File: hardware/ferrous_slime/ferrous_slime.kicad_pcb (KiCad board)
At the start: 2 copper layers, 41.4 x 34 mm, 50 parts, among them J1 IMU_Connector, J2 Battery_Connector, J3 USB_C_Receptacle_USB2.0, Q1 DMG3415U, SW1 SW_PWR, U1 BNO/MPU/ICM_Break, U2 ESP32-C3-MINI-1, U3 TP4056, U4 M3406, Y1 32.768Hz

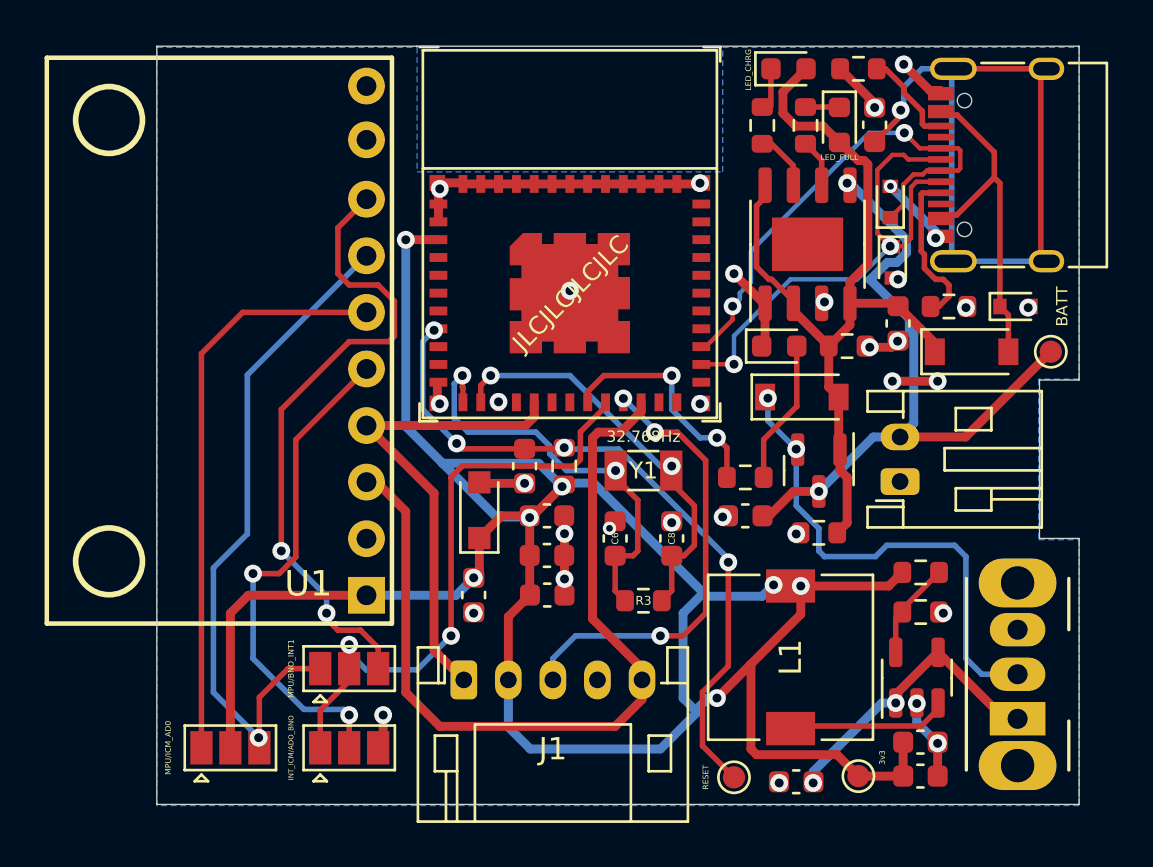
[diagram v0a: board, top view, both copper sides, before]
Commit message: Removed gerbers, made some minor tweaks to board layout
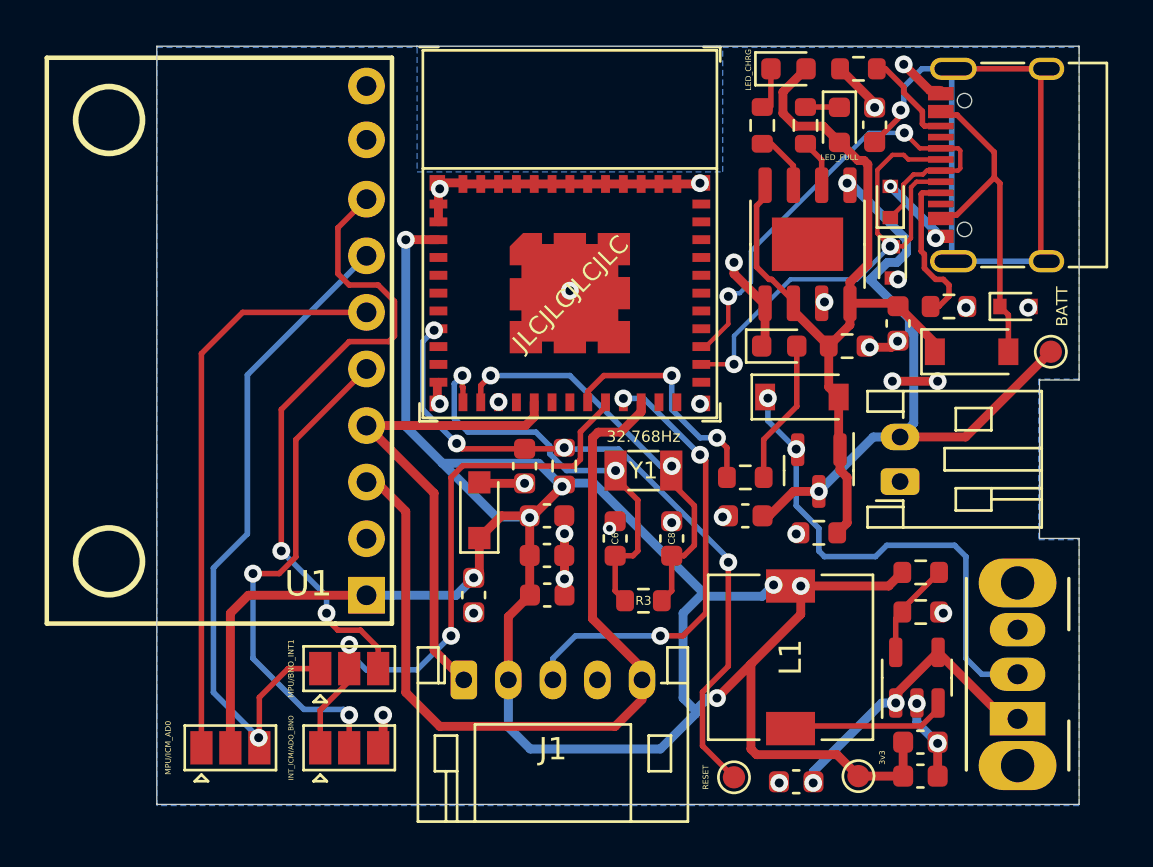
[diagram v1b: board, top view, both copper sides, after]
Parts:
- D5: value PROG_LED -> LED

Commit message: Optimized signal traces and ground fills
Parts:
- moved C4 6.07 mm to (67.5, 48.7), turned to -90 degrees
- moved J2 0.19 mm to (89.0, 49.3)
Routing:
- net USB_D+: track 22.4 -> 25.3 mm
- net USB_D-: track 22.6 -> 25.0 mm
- net GND: track 63.7 -> 65.0 mm, vias 32 -> 46
- net IO6_INT1: track 25.5 -> 26.6 mm
- net Net-(JP1-Pad3): track 30.9 -> 30.0 mm
- net IO8_SCL: track 37.0 -> 36.4 mm
- net +BATT: track 30.6 -> 30.7 mm, vias 2 -> 3
- net +3V3: track 109.8 -> 109.7 mm, vias 7 -> 8
- added copper zone on F.Cu, net GND
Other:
- outline, holes or cut-outs redrawn

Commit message: breakout_slime v0.1.2
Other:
- board text added: "${REVISION}"
- board text added: "ferrous_slime ${REVISION} by TheButlah License: CERN-OHL-P v2 or later github.com/TheButlah/slimevr_pcb"
- board text removed: "License: CERN-OHL-P v2 or later github.com/TheButlah/slimevr_pcb"
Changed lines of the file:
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@@
     (title "ferrous_slime")
     (date "2022-03-07")
+    (rev "v0.0.0")
     (company "github.com/thebutlah/slimevr_pcb")
     (comment 1 "Licensed under CERN-OHL-P v2 or later")
@@
       (xy 97.2312 29.919)
     ) (layer "Edge.Cuts") (width 0.05) (fill none))
-  (gr_text "License: CERN-OHL-P v2 or later\ngithub.com/TheButlah/slimevr_pcb" (at 58.166 44.196 90) (layer "B.SilkS")
+  (gr_text "ferrous_slime ${REVISION} by TheButlah\nLicense: CERN-OHL-P v2 or later\ngithub.com/TheButlah/slimevr_pcb\n" (at 58.801 44.069 90) (layer "B.SilkS")
     (effects (font (size 1 1) (thickness 0.2)) (justify mirror))
+  )
+  (gr_text "${REVISION}" (at 56.769 30.861 270) (layer "F.SilkS")
+    (effects (font (size 1 1) (thickness 0.2)) (justify left))
   )
   (gr_text "JLCJLCJLCJLC" (at 74.201188 41.015404 45) (layer "F.SilkS")
@@
     (pts (xy 97.028 29.919) (xy 55.626 29.919))
     (height 4.519)
-    (gr_text "41.4020 mm" (at 76.327 24.25) (layer "Dwgs.User")
+    (gr_text "1630.0000 mils" (at 76.327 24.25) (layer "Dwgs.User")
       (effects (font (size 1 1) (thickness 0.15)))
     )
@@
     (pts (xy 55.626 63.955) (xy 55.626 29.919))
     (height -9.906)
-    (gr_text "34.0360 mm" (at 44.57 46.937 90) (layer "Dwgs.User")
+    (gr_text "1340.0000 mils" (at 44.57 46.937 90) (layer "Dwgs.User")
       (effects (font (size 1 1) (thickness 0.15)))
     )
@@
     (pts (xy 97.028 29.919) (xy 50.52 29.972))
     (height 1.775074)
-    (gr_text "46.5080 mm" (at 73.770666 27.020428 0.06529360539) (layer "Dwgs.User")
-      (effects (font (size 1 1) (thickness 0.15)))
-    )
+    (gr_text "1831.0248 mils" (at 73.770666 27.020428 0.06529360539) (layer "Dwgs.User")
+      (effects (font (size 1 1) (thickness 0.15)))
+    )

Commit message: Added battery sense to ferrous_slime
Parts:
- removed C10: 470nF, Capacitor_SMD:C_0603_1608Metric
- added R12: 1M, Resistor_SMD:R_0603_1608Metric, F.Cu at (87.9, 33.5)
- added R13: 120K 1%, Resistor_SMD:R_0603_1608Metric, F.Cu at (72.5, 55.0)
- added R14: 30K 1%, Resistor_SMD:R_0603_1608Metric, F.Cu at (71.0, 55.0)
- R7: value 470R 1% -> 1K
- moved C5 10.2 mm to (60.0, 56.9), turned to 0 degrees
- moved C3 1.16 mm to (73.8, 51.8), turned to -90 degrees
- moved C1 1.10 mm to (74.2, 55.0), turned to 90 degrees
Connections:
- U2 pad 6: unconnected-(U2-Pad6) -> B_SENSE
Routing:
- net +BATT: track 30.7 -> 63.4 mm, vias 3 -> 5
- net B_SENSE: track 0.00 -> 17.6 mm, vias 0 -> 2
- net +3V3: track 109.7 -> 107.0 mm
- net GND: track 65.0 -> 65.8 mm
- net IO7_INT2: track 20.4 -> 21.0 mm

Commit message: Added breakouts for remaining unused IO
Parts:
- added J4: Unused_IO, Connector_PinHeader_2.54mm:PinHeader_1x07_P2.54mm_Vertical, F.Cu at (57.8, 34.4)
- R12: value 1M -> 120K
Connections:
- U2 pad 18: unconnected-(U2-Pad18) -> UNUSED_IO4
- U2 pad 23: unconnected-(U2-Pad23) -> UNUSED_IO9
- U2 pad 30: unconnected-(U2-Pad30) -> UNUSED_IO20
- U2 pad 31: unconnected-(U2-Pad31) -> UNUSED_IO21
- U2 pad 5: unconnected-(U2-Pad5) -> UNUSED_IO2
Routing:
- net UNUSED_IO21: track 0.00 -> 48.1 mm, vias 0 -> 2
- net UNUSED_IO20: track 0.00 -> 42.9 mm, vias 0 -> 1
- net UNUSED_IO9: track 0.00 -> 30.9 mm, vias 0 -> 2
- net UNUSED_IO4: track 0.00 -> 23.4 mm, vias 0 -> 1
- net UNUSED_IO2: track 0.00 -> 18.2 mm, vias 0 -> 2
- net +3V3: track 107.0 -> 122.9 mm
- net GND: track 65.8 -> 58.4 mm, vias 46 -> 48
- net Net-(C2-Pad1): track 30.9 -> 33.1 mm
- net IO0: track 18.6 -> 19.9 mm
- net Net-(JP1-Pad3): track 30.0 -> 31.3 mm
- net IO5_LED: track 10.6 -> 9.82 mm
- net IO7_INT2: track 21.0 -> 21.7 mm
- net Net-(JP1-Pad1): track 25.9 -> 25.3 mm

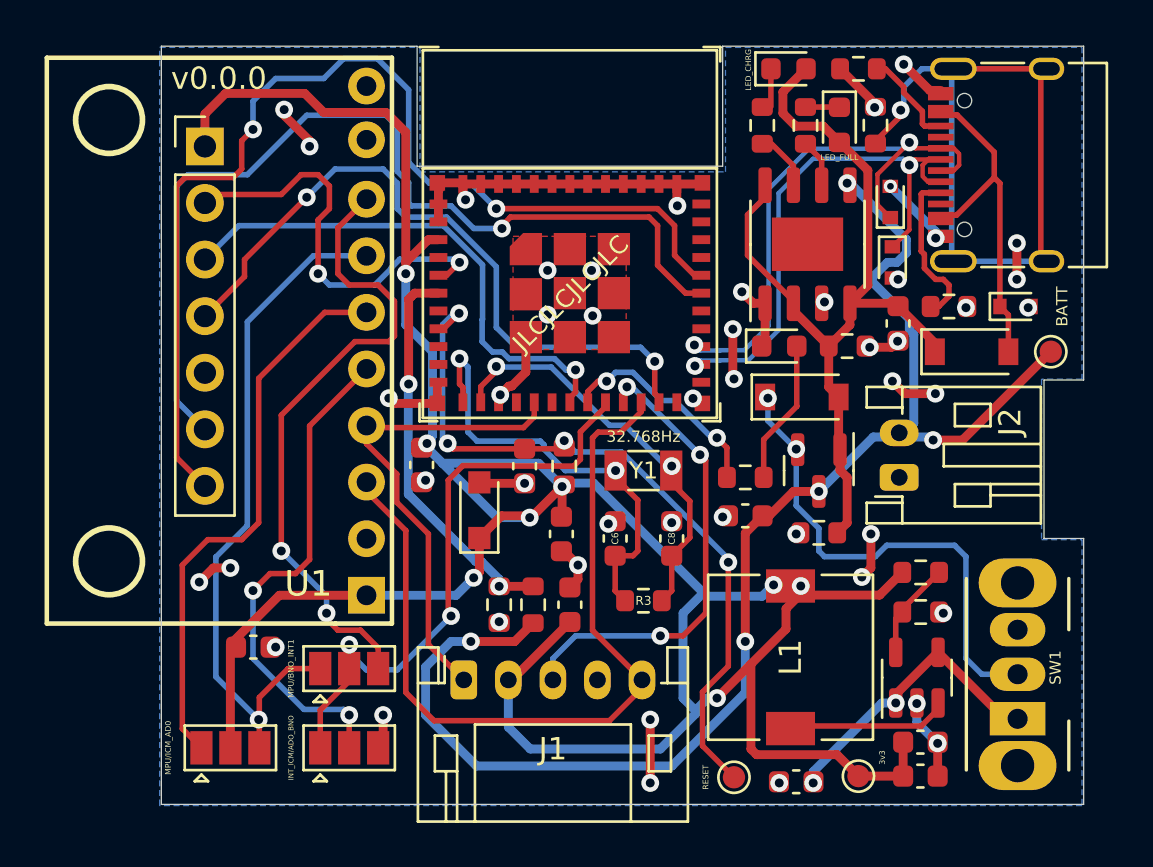
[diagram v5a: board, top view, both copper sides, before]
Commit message: Fixed jumper silkscreens and added double ground plane
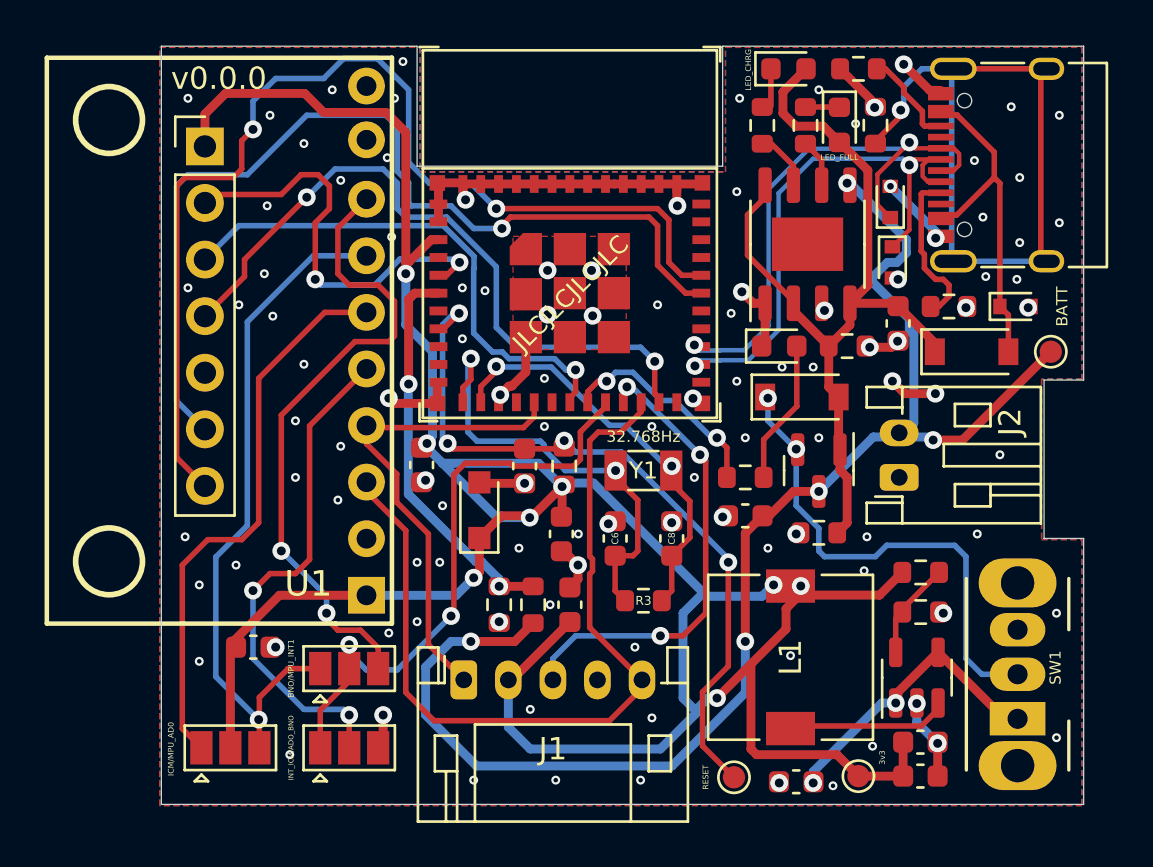
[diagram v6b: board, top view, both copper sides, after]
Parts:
- JP1: value MPU/ICM_AD0 -> ICM/MPU_AD0
- JP3: value MPU/BNO_INT1 -> BNO/MPU_INT1
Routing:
- net GND: track 58.4 -> 45.8 mm, vias 48 -> 111

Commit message: Annotated pins and added silkscreen art
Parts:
- added G***: LOGO, slimevr_pcb:dancing_ferris, B.Cu at (81.2, 48.0)
- J4: footprint Connector_PinHeader_2.54mm:PinHeader_1x07_P2.54mm_Vertical -> slimevr_pcb:IO_Breakouts
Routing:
- net +BATT: track 63.4 -> 65.1 mm
- net GND: vias 111 -> 110
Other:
- board text added: "3v3"
- board text added: "B+"
- board text added: "GND"
- board text added: "INT2"
- board text added: "SCL"
- board text added: "SDA"

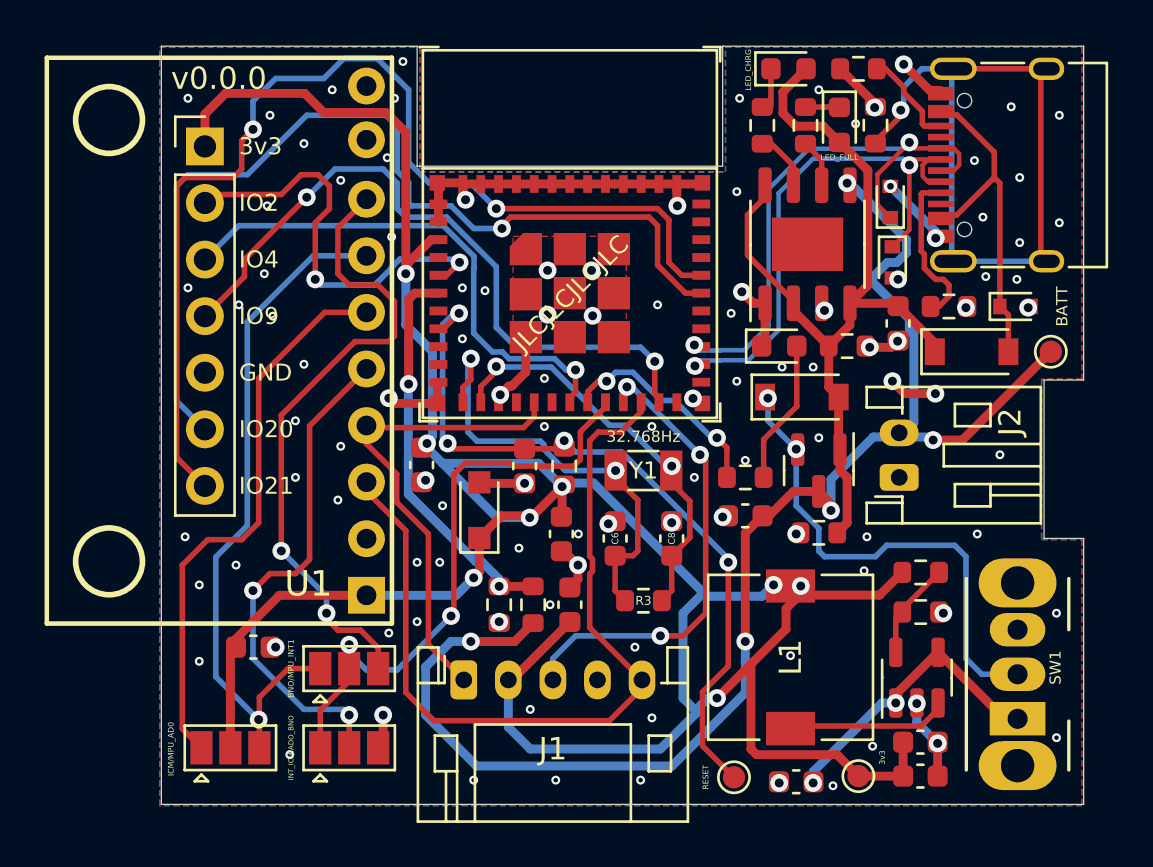
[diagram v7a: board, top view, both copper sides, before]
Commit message: Removed Rust_Board and updated all renders/plots
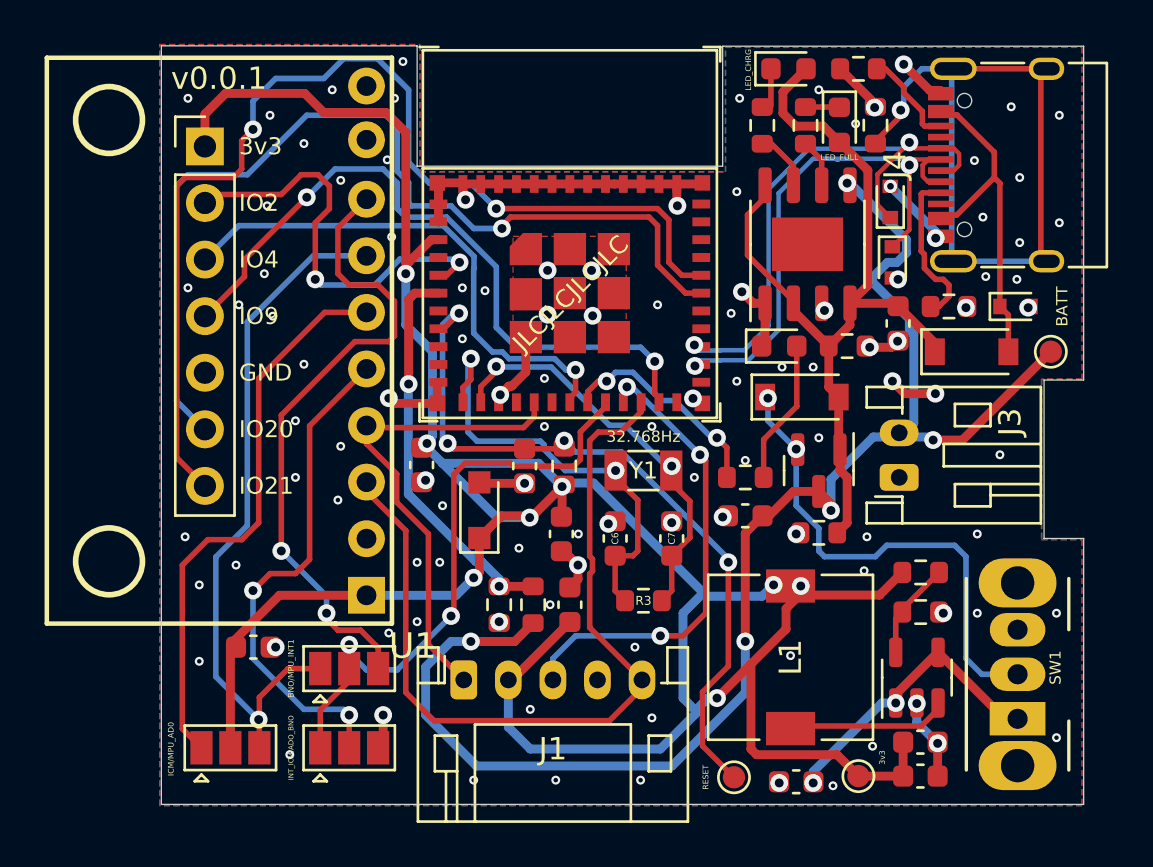
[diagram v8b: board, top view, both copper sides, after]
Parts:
- R2: value 1.66K -> 2K
- renumbered C11 to C10, C12 to C11, C13 to C12, C8 to C7, C7 to C8, J4 to J2, J2 to J3, J3 to J4, R14 to R10, R8 to R11, R9 to R12, R10 to R13, R11 to R14, R12 to R8, R13 to R9
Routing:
- net GND: vias 110 -> 111
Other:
- board size 41.4 x 34 mm -> 41.4 x 34.1 mm
